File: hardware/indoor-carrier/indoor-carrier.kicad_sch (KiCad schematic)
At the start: 29 parts, among them J1 24 VAC, J2 Mode in 24 VAC, J3 DS18B20 supply air, J4 DS18B20 return air, J5 I2C expansion, U1 ESP32 DevKit, U2 LM2596HV, U3 H11AA1, U4 H11AA1, U5 H11AA1, U6 H11AA1

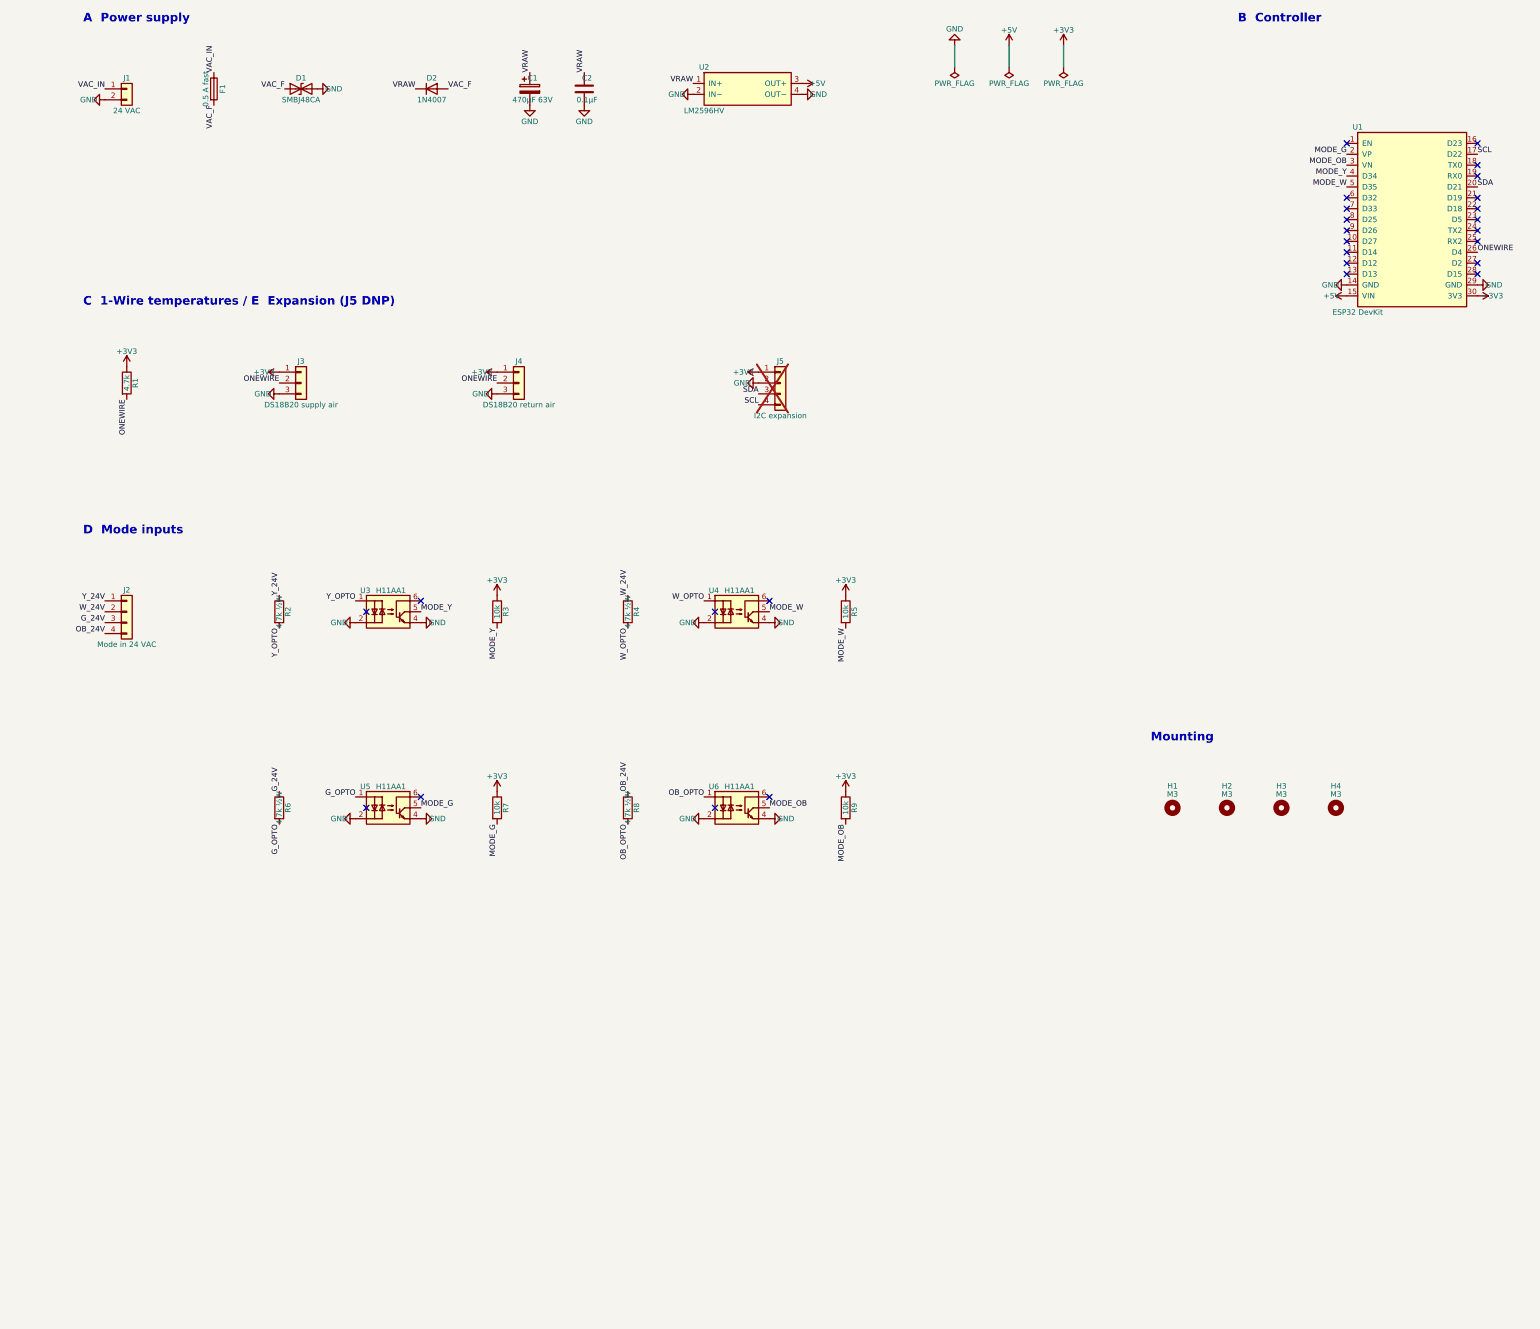
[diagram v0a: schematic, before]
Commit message: Rev B schematics: Wio-SX1262 footprint, flattened AMS1117 symbol, ERC clean
gen_footprints.py: Wio_SX1262 from the Seeed datasheet V1.0 figure 9 (pins 1-8 on
one edge, 12..9 on the other, counter-clockwise; matches design.lora_section and
figure 2). Pads 0.6 x 3.0 mm, 0.8 mm longer outward than the datasheet's 2.2 for hand
soldering; courtyard runs 5 mm past the u.FL side for the plug and pigtail.
gen_sch.py: flatten derived library symbols (AMS1117-3.3 extends AP1117-15), keep
field justification. check_netlist.py: letter pin numbers (audio jack S/T/R) and the
Wio module in the connector summary. design.py: LoRa section spaced out on the sheet.
Checked against KiCad 10: TCA9548APWR pins match MUX_PINS / A0-A2 / RESET / SDA /
SCL / VCC; AudioJack3 S/T/R match the SJ1-3523N pads; AMS1117 1 GND 2 VO 3 VI;
every footprint in design.py exists. ERC 0 errors 0 warnings on both boards.

Co-Authored-By: Claude Opus 5.5 (1M context) <noreply@anthropic.com>
Claude-Session: https://claude.ai/code/session_01V4kWJ9CiBrt94u4WqUxFsk
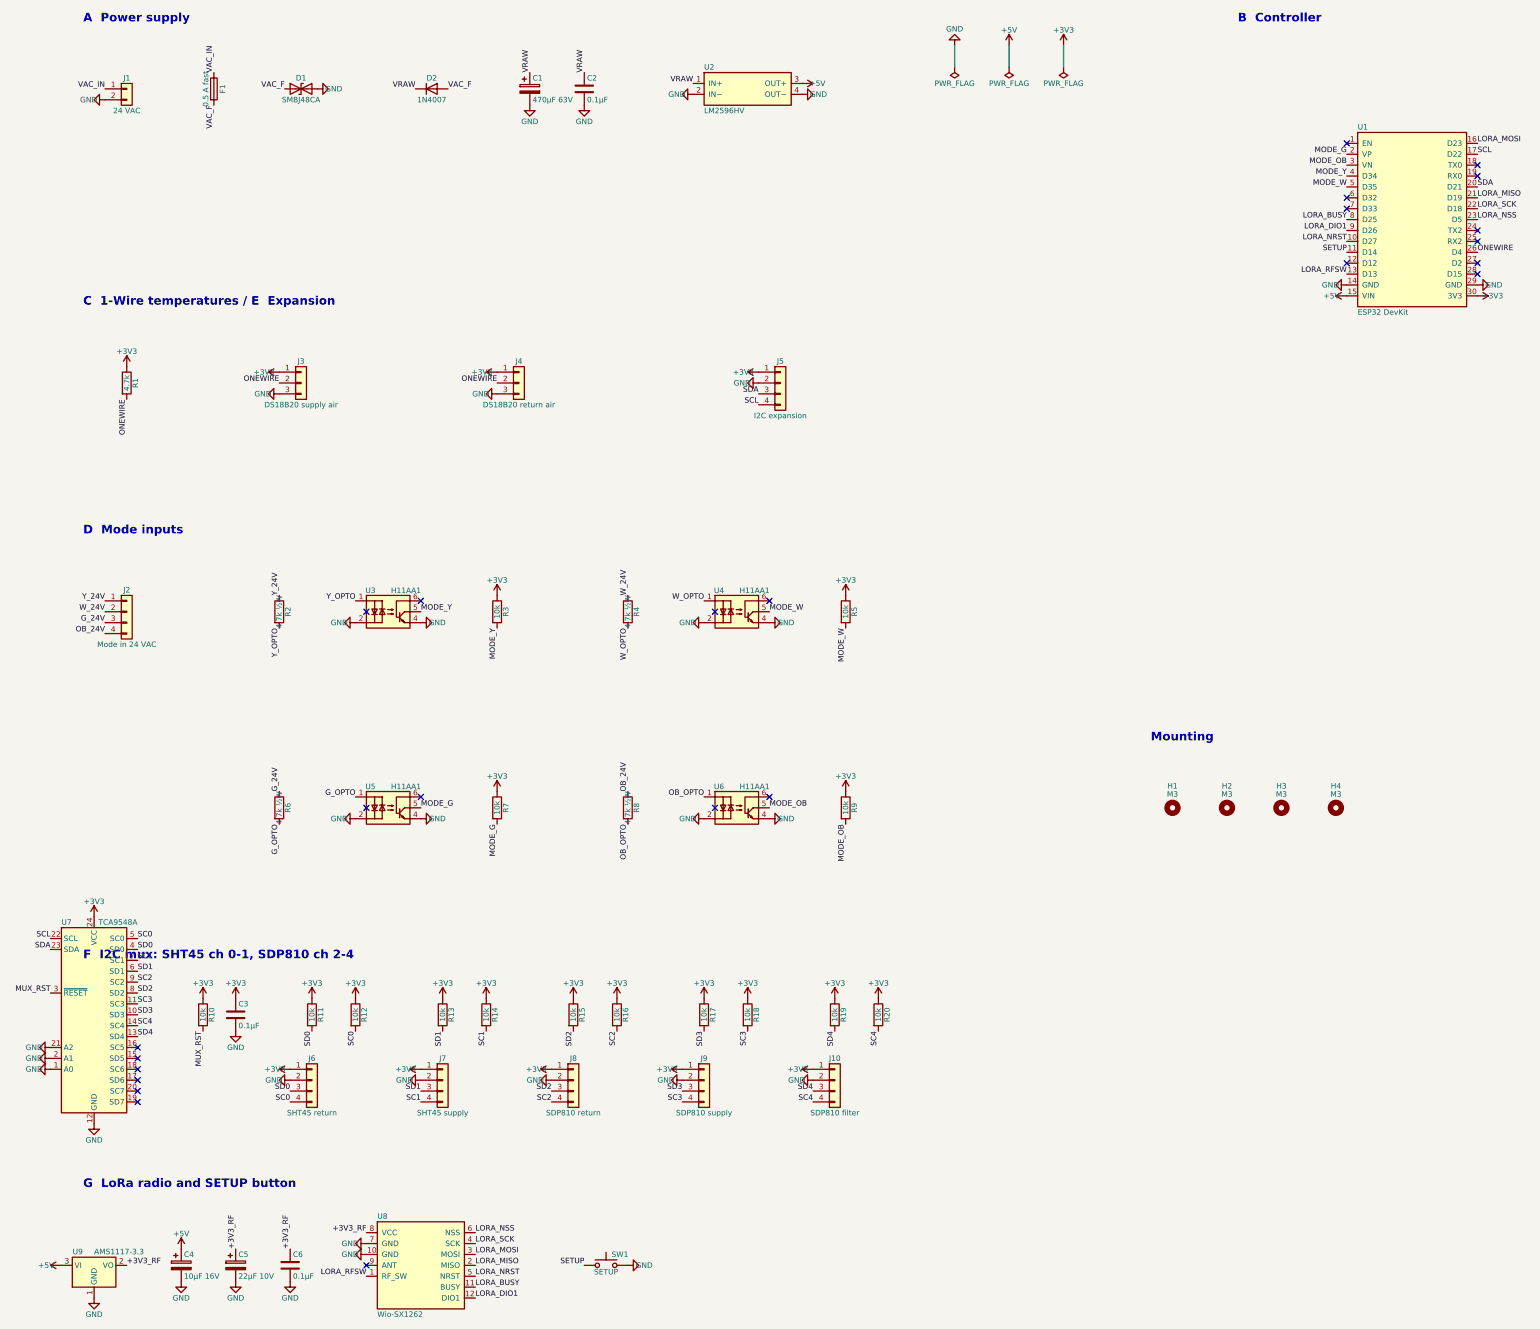
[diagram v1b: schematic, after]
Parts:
- added C3: 0.1µF, Capacitor_SMD:C_0805_2012Metric_Pad1.18x1.45mm_HandSolder, symbol Device:C
- added C4: 10µF 16V, Capacitor_THT:CP_Radial_D5.0mm_P2.00mm, symbol Device:C_Polarized
- added C5: 22µF 10V, Capacitor_THT:CP_Radial_D5.0mm_P2.00mm, symbol Device:C_Polarized
- added C6: 0.1µF, Capacitor_THT:C_Disc_D5.0mm_W2.5mm_P2.50mm, symbol Device:C
- added J10: SDP810 filter, Connector_JST:JST_XH_B4B-XH-A_1x04_P2.50mm_Vertical, symbol Connector_Generic:Conn_01x04
- added J6: SHT45 return, Connector_JST:JST_XH_B4B-XH-A_1x04_P2.50mm_Vertical, symbol Connector_Generic:Conn_01x04
- added J7: SHT45 supply, Connector_JST:JST_XH_B4B-XH-A_1x04_P2.50mm_Vertical, symbol Connector_Generic:Conn_01x04
- added J8: SDP810 return, Connector_JST:JST_XH_B4B-XH-A_1x04_P2.50mm_Vertical, symbol Connector_Generic:Conn_01x04
- added J9: SDP810 supply, Connector_JST:JST_XH_B4B-XH-A_1x04_P2.50mm_Vertical, symbol Connector_Generic:Conn_01x04
- added R10, R11, R12, R13, R14, R15, R16, R17, R18, R19, R20: 10k, Resistor_SMD:R_0805_2012Metric_Pad1.20x1.40mm_HandSolder, symbol Device:R
- added SW1: SETUP, Button_Switch_THT:SW_PUSH_6mm, symbol Switch:SW_Push
- added U7: TCA9548A, Package_SO:TSSOP-24_4.4x7.8mm_P0.65mm, symbol Interface_Expansion:TCA9548APWR
- added U8: Wio-SX1262, hvac_carrier:Wio_SX1262, symbol hvac_carrier:Wio_SX1262
- added U9: AMS1117-3.3, Package_TO_SOT_SMD:SOT-223-3_TabPin2, symbol Regulator_Linear:AMS1117-3.3
- J5: now fitted
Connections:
- net +3V3: now also C3.1, J10.1 (Pin_1), J6.1 (Pin_1), J7.1 (Pin_1), J8.1 (Pin_1), J9.1 (Pin_1), R10.1, R11.1, R12.1, R13.1, R14.1, R15.1, R16.1, R17.1, R18.1, R19.1, R20.1, U7.24 (VCC)
- net +5V: now also C4.1, U9.3 (VI)
- net GND: now also C3.2, C4.2, C5.2, C6.2, J10.2 (Pin_2), J6.2 (Pin_2), J7.2 (Pin_2), J8.2 (Pin_2), J9.2 (Pin_2), SW1.2, U7.1 (A0), U7.12 (GND), U7.2 (A1), U7.21 (A2), U8.10 (GND), U8.7 (GND), U9.1 (GND)
- net SCL: now also U7.22 (SCL)
- net SDA: now also U7.23 (SDA)
- net LORA_NRST: now reaches U1.10 (D27)
- net LORA_NRST: now also U8.5 (NRST)
- net SETUP: now reaches U1.11 (D14)
- net SETUP: now also SW1.1
- net LORA_RFSW: now reaches U1.13 (D13)
- net LORA_RFSW: now also U8.1 (RF_SW)
- net LORA_MOSI: now reaches U1.16 (D23)
- net LORA_MOSI: now also U8.3 (MOSI)
- net LORA_MISO: now reaches U1.21 (D19)
- net LORA_MISO: now also U8.2 (MISO)
- net LORA_SCK: now reaches U1.22 (D18)
- net LORA_SCK: now also U8.4 (SCK)
- net LORA_NSS: now reaches U1.23 (D5)
- net LORA_NSS: now also U8.6 (NSS)
- net LORA_BUSY: now reaches U1.8 (D25)
- net LORA_BUSY: now also U8.11 (BUSY)
- net LORA_DIO1: now reaches U1.9 (D26)
- net LORA_DIO1: now also U8.12 (DIO1)
- new net +3V3_RF: C5.1, C6.1, U8.8 (VCC), U9.2 (VO)
- new net MUX_RST: R10.2, U7.3 (~{RESET})
- new net SC0: J6.4 (Pin_4), R12.2, U7.5 (SC0)
- new net SC1: J7.4 (Pin_4), R14.2, U7.7 (SC1)
- new net SC2: J8.4 (Pin_4), R16.2, U7.9 (SC2)
- new net SC3: J9.4 (Pin_4), R18.2, U7.11 (SC3)
- new net SC4: J10.4 (Pin_4), R20.2, U7.14 (SC4)
- new net SD0: J6.3 (Pin_3), R11.2, U7.4 (SD0)
- new net SD1: J7.3 (Pin_3), R13.2, U7.6 (SD1)
- new net SD2: J8.3 (Pin_3), R15.2, U7.8 (SD2)
- new net SD3: J9.3 (Pin_3), R17.2, U7.10 (SD3)
- new net SD4: J10.3 (Pin_3), R19.2, U7.13 (SD4)
- no-connect marks 27 -> 25
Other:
- note added: "C 1-Wire temperatures / E Expansion"
- note added: "F I2C mux: SHT45 ch 0-1, SDP810 ch 2-4"
- note added: "G LoRa radio and SETUP button"
- note removed: "C 1-Wire temperatures / E Expansion (J5 DNP)"
